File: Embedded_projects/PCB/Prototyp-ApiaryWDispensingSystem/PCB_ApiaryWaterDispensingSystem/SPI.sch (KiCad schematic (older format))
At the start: 8 parts

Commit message: added lot of changes to project #3
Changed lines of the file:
@@
 $Descr A4 11693 8268
 encoding utf-8
-Sheet 6 7
+Sheet 6 9
 Title ""
 Date ""
@@
 $EndComp
 $Comp
-L power:+3.3V #PWR?
+L power:+3.3V #PWR0174
 U 1 1 67E4A022
 P 5230 860
-F 0 "#PWR?" H 5230 710 50  0001 C CNN
+F 0 "#PWR0174" H 5230 710 50  0001 C CNN
 F 1 "+3.3V" H 5245 1033 50  0000 C CNN
 F 2 "" H 5230 860 50  0001 C CNN
@@
 $EndComp
 $Comp
-L power:+3.3V #PWR?
+L power:+3.3V #PWR0175
 U 1 1 67E56C81
 P 940 600
-F 0 "#PWR?" H 940 450 50  0001 C CNN
+F 0 "#PWR0175" H 940 450 50  0001 C CNN
 F 1 "+3.3V" H 730 650 50  0000 C CNN
 F 2 "" H 940 600 50  0001 C CNN
@@
 Text GLabel 1010 2770 0    50   Input ~ 0
 CD
+Text HLabel 1510 2170 2    50   Input ~ 0
+SPI3_SCK
+Text HLabel 1510 2270 2    50   Input ~ 0
+SPI3_MOSI
+Text HLabel 1510 2370 2    50   Input ~ 0
+SPI3_MISO
+Text HLabel 1520 2670 2    50   Input ~ 0
+SPI3_CS
+Wire Wire Line
+	1510 2170 970  2170
+Wire Wire Line
+	1510 2270 990  2270
+Wire Wire Line
+	1510 2370 1010 2370
+Wire Wire Line
+	1520 2670 1010 2670
 $EndSCHEMATC

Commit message: Many design changes have been added over the past few months #3
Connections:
- no-connect marks 0 -> 3
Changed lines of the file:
@@
 $Descr A4 11693 8268
 encoding utf-8
-Sheet 6 9
+Sheet 5 9
 Title ""
 Date ""
@@
 Wire Wire Line
 	1520 2670 1010 2670
+NoConn ~ 1010 2470
+NoConn ~ 1010 2570
+NoConn ~ 1010 2770
 $EndSCHEMATC

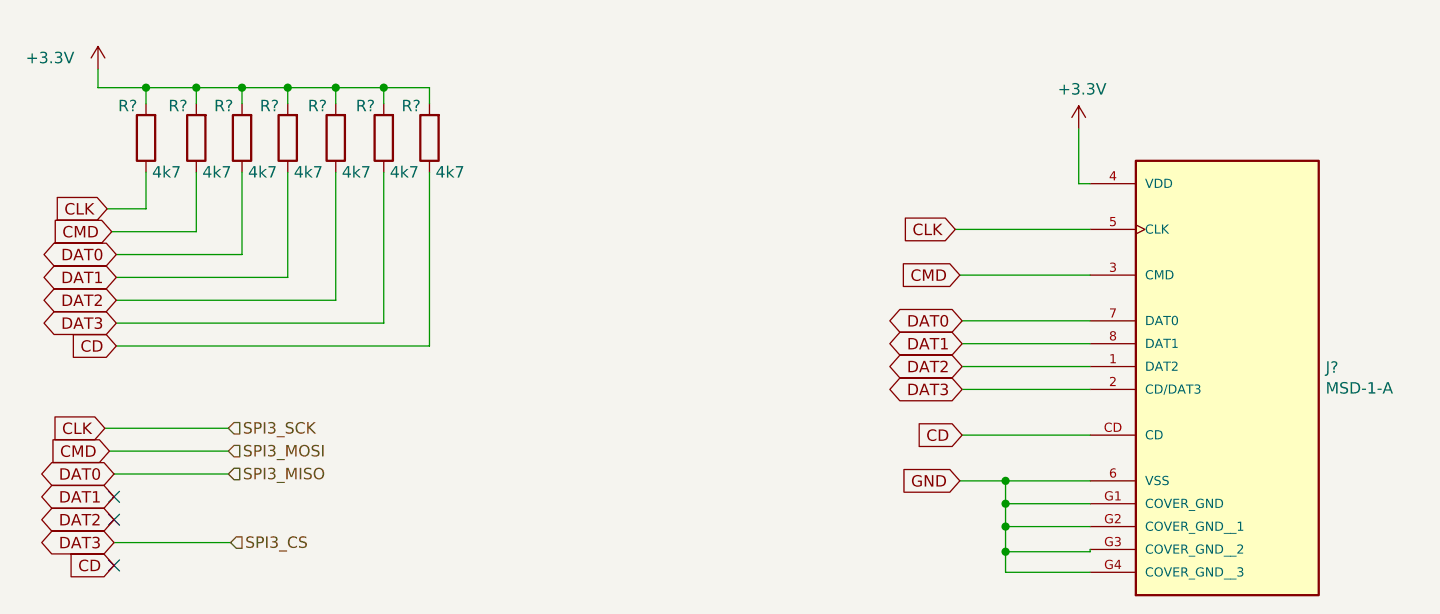
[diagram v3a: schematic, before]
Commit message: All signal has been routed, the analog part needs to be completed
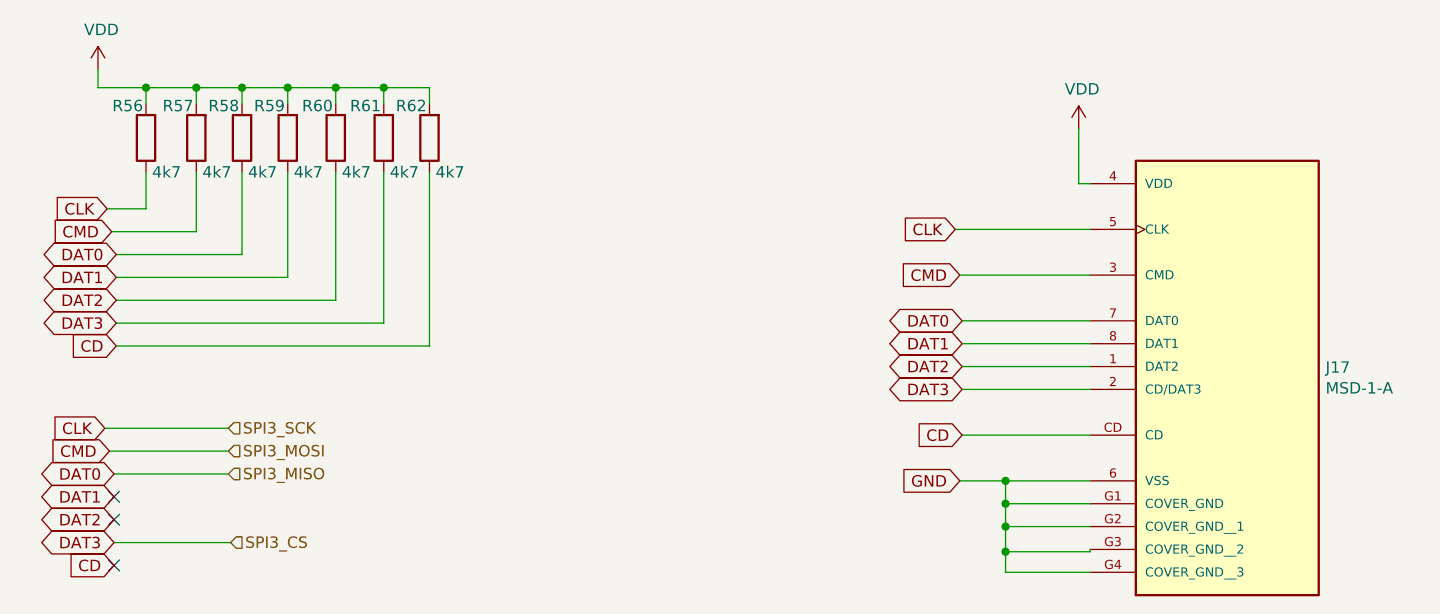
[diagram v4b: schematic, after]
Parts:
- R56, R57, R58, R59, R60, R61, R62: renamed from R?; footprint (none) -> Resistor_SMD:R_0603_1608Metric
- gave numbers to parts that had none: 1
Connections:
- net +3V3 renamed VDD
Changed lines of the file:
@@
 $EndDescr
 $Comp
-L ApiaryWaterDispensingSystem:MSD-1-A J?
+L ApiaryWaterDispensingSystem:MSD-1-A J17
 U 1 1 67E48E17
 P 5880 1800
-F 0 "J?" H 6310 1696 50  0000 L CNN
+F 0 "J17" H 6310 1696 50  0000 L CNN
 F 1 "MSD-1-A" H 6310 1605 50  0000 L CNN
 F 2 "CUI_MSD-1-A" H 5880 1800 50  0001 L BNN
@@
 F 7 "CUI Devices" H 5880 1800 50  0001 L BNN "MANUFACTURER"
 	1    5880 1800
-	1    0    0    -1
-$EndComp
-$Comp
-L power:+3.3V #PWR0174
-U 1 1 67E4A022
-P 5230 860
-F 0 "#PWR0174" H 5230 710 50  0001 C CNN
-F 1 "+3.3V" H 5245 1033 50  0000 C CNN
-F 2 "" H 5230 860 50  0001 C CNN
-F 3 "" H 5230 860 50  0001 C CNN
-	1    5230 860
 	1    0    0    -1
 $EndComp
@@
 	4910 2500 4910 2600
 Wire Wire Line
-	5230 860  5230 1100
-Wire Wire Line
 	5230 1100 5280 1100
 Wire Wire Line
@@
 CD
 $Comp
-L Device:R R?
+L Device:R R56
 U 1 1 67E52805
 P 1150 900
-F 0 "R?" H 1230 760 50  0000 C CNN
+F 0 "R56" H 1230 760 50  0000 C CNN
 F 1 "4k7" H 1060 1050 50  0000 C CNN
-F 2 "" V 1080 900 50  0001 C CNN
+F 2 "Resistor_SMD:R_0603_1608Metric" V 1080 900 50  0001 C CNN
 F 3 "~" H 1150 900 50  0001 C CNN
 	1    1150 900
@@
 $EndComp
 $Comp
-L Device:R R?
+L Device:R R57
 U 1 1 67E555EB
 P 1370 900
-F 0 "R?" H 1450 760 50  0000 C CNN
+F 0 "R57" H 1450 760 50  0000 C CNN
 F 1 "4k7" H 1280 1050 50  0000 C CNN
-F 2 "" V 1300 900 50  0001 C CNN
+F 2 "Resistor_SMD:R_0603_1608Metric" V 1300 900 50  0001 C CNN
 F 3 "~" H 1370 900 50  0001 C CNN
 	1    1370 900
@@
 $EndComp
 $Comp
-L power:+3.3V #PWR0175
-U 1 1 67E56C81
-P 940 600
-F 0 "#PWR0175" H 940 450 50  0001 C CNN
-F 1 "+3.3V" H 730 650 50  0000 C CNN
-F 2 "" H 940 600 50  0001 C CNN
-F 3 "" H 940 600 50  0001 C CNN
-	1    940  600
-	1    0    0    -1
-$EndComp
-$Comp
-L Device:R R?
+L Device:R R58
 U 1 1 67E57EDA
 P 1570 900
-F 0 "R?" H 1650 760 50  0000 C CNN
+F 0 "R58" H 1650 760 50  0000 C CNN
 F 1 "4k7" H 1480 1050 50  0000 C CNN
-F 2 "" V 1500 900 50  0001 C CNN
+F 2 "Resistor_SMD:R_0603_1608Metric" V 1500 900 50  0001 C CNN
 F 3 "~" H 1570 900 50  0001 C CNN
 	1    1570 900
@@
 $EndComp
 $Comp
-L Device:R R?
+L Device:R R59
 U 1 1 67E582FC
 P 1770 900
-F 0 "R?" H 1850 760 50  0000 C CNN
+F 0 "R59" H 1850 760 50  0000 C CNN
 F 1 "4k7" H 1680 1050 50  0000 C CNN
-F 2 "" V 1700 900 50  0001 C CNN
+F 2 "Resistor_SMD:R_0603_1608Metric" V 1700 900 50  0001 C CNN
 F 3 "~" H 1770 900 50  0001 C CNN
 	1    1770 900
@@
 $EndComp
 $Comp
-L Device:R R?
+L Device:R R60
 U 1 1 67E58522
 P 1980 900
-F 0 "R?" H 2060 760 50  0000 C CNN
+F 0 "R60" H 2060 760 50  0000 C CNN
 F 1 "4k7" H 1890 1050 50  0000 C CNN
-F 2 "" V 1910 900 50  0001 C CNN
+F 2 "Resistor_SMD:R_0603_1608Metric" V 1910 900 50  0001 C CNN
 F 3 "~" H 1980 900 50  0001 C CNN
 	1    1980 900
@@
 Connection ~ 1770 680
 $Comp
-L Device:R R?
+L Device:R R61
 U 1 1 67E5E749
 P 2190 900
-F 0 "R?" H 2270 760 50  0000 C CNN
+F 0 "R61" H 2270 760 50  0000 C CNN
 F 1 "4k7" H 2100 1050 50  0000 C CNN
-F 2 "" V 2120 900 50  0001 C CNN
+F 2 "Resistor_SMD:R_0603_1608Metric" V 2120 900 50  0001 C CNN
 F 3 "~" H 2190 900 50  0001 C CNN
 	1    2190 900
@@
 $EndComp
 $Comp
-L Device:R R?
+L Device:R R62
 U 1 1 67E5E9E5
 P 2390 900
-F 0 "R?" H 2470 760 50  0000 C CNN
+F 0 "R62" H 2470 760 50  0000 C CNN
 F 1 "4k7" H 2300 1050 50  0000 C CNN
-F 2 "" V 2320 900 50  0001 C CNN
+F 2 "Resistor_SMD:R_0603_1608Metric" V 2320 900 50  0001 C CNN
 F 3 "~" H 2390 900 50  0001 C CNN
 	1    2390 900
@@
 NoConn ~ 1010 2570
 NoConn ~ 1010 2770
+$Comp
+L power:VDD #PWR0125
+U 1 1 690DEBF7
+P 940 600
+F 0 "#PWR0125" H 940 450 50  0001 C CNN
+F 1 "VDD" H 955 773 50  0000 C CNN
+F 2 "" H 940 600 50  0001 C CNN
+F 3 "" H 940 600 50  0001 C CNN
+	1    940  600
+	1    0    0    -1
+$EndComp
+Wire Wire Line
+	5230 860  5230 1100
+$Comp
+L power:VDD #PWR0126
+U 1 1 690E00FD
+P 5230 860
+F 0 "#PWR0126" H 5230 710 50  0001 C CNN
+F 1 "VDD" H 5245 1033 50  0000 C CNN
+F 2 "" H 5230 860 50  0001 C CNN
+F 3 "" H 5230 860 50  0001 C CNN
+	1    5230 860
+	1    0    0    -1
+$EndComp
 $EndSCHEMATC
